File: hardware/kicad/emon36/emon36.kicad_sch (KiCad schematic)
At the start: 39 parts, among them J1 Barrel_Jack, J37 USB_B_Micro, SW1 SW_MEC_5E, SW2 SW_MEC_5E, SW3 SW_MEC_5E, SW4 SW_MEC_5E, SW5 SW_MEC_5E, SW6 SW_MEC_5E, U1 ESP32-C3-WROOM-02-N4, U8 TPS54233

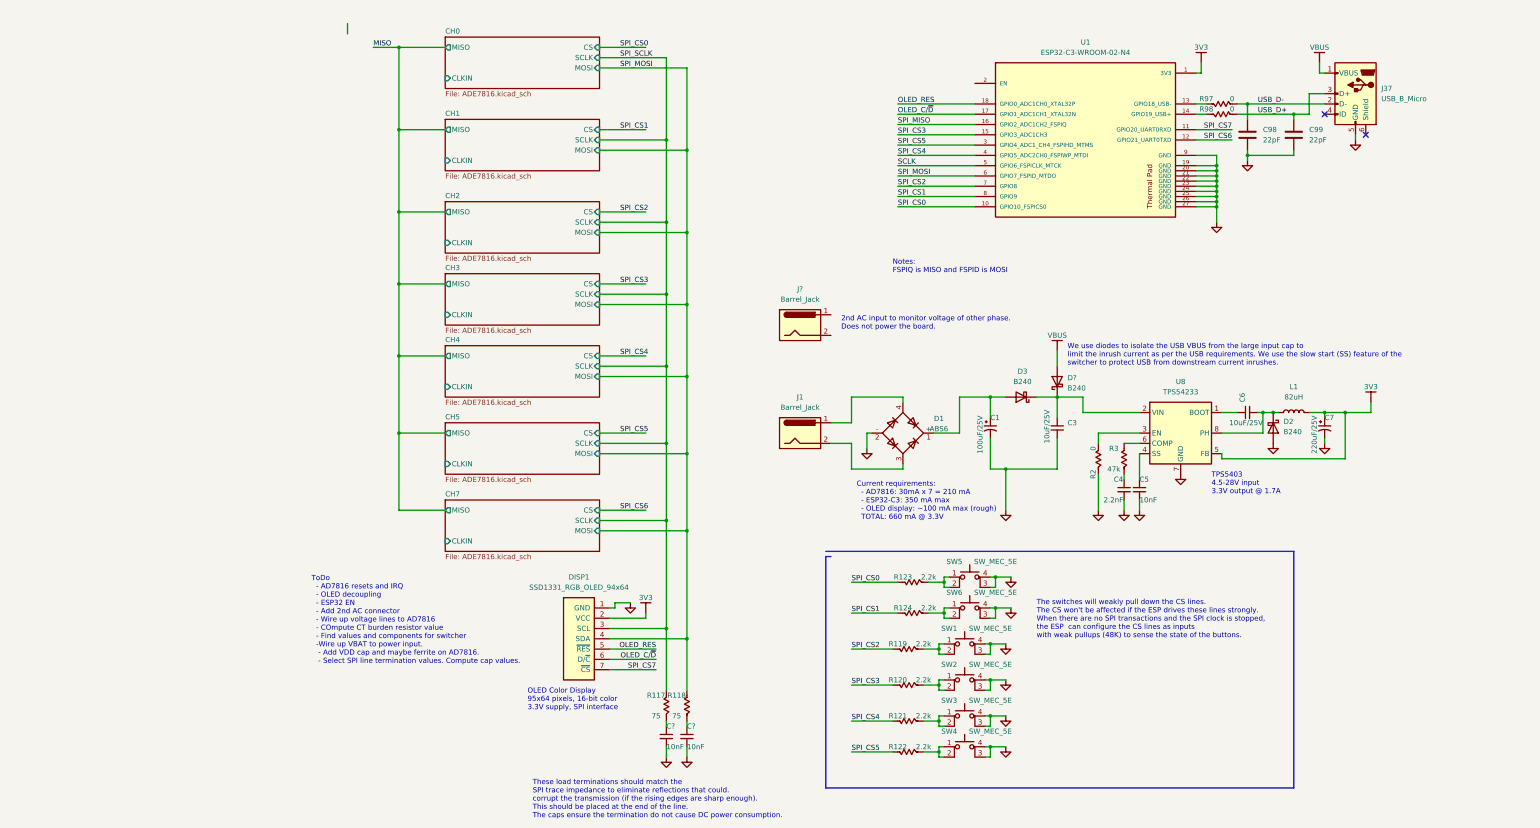
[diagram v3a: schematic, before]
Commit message: Another major schematics/PCB iteration. Added decoupling caps, interrupts, etc. Improved power system. Added clock.
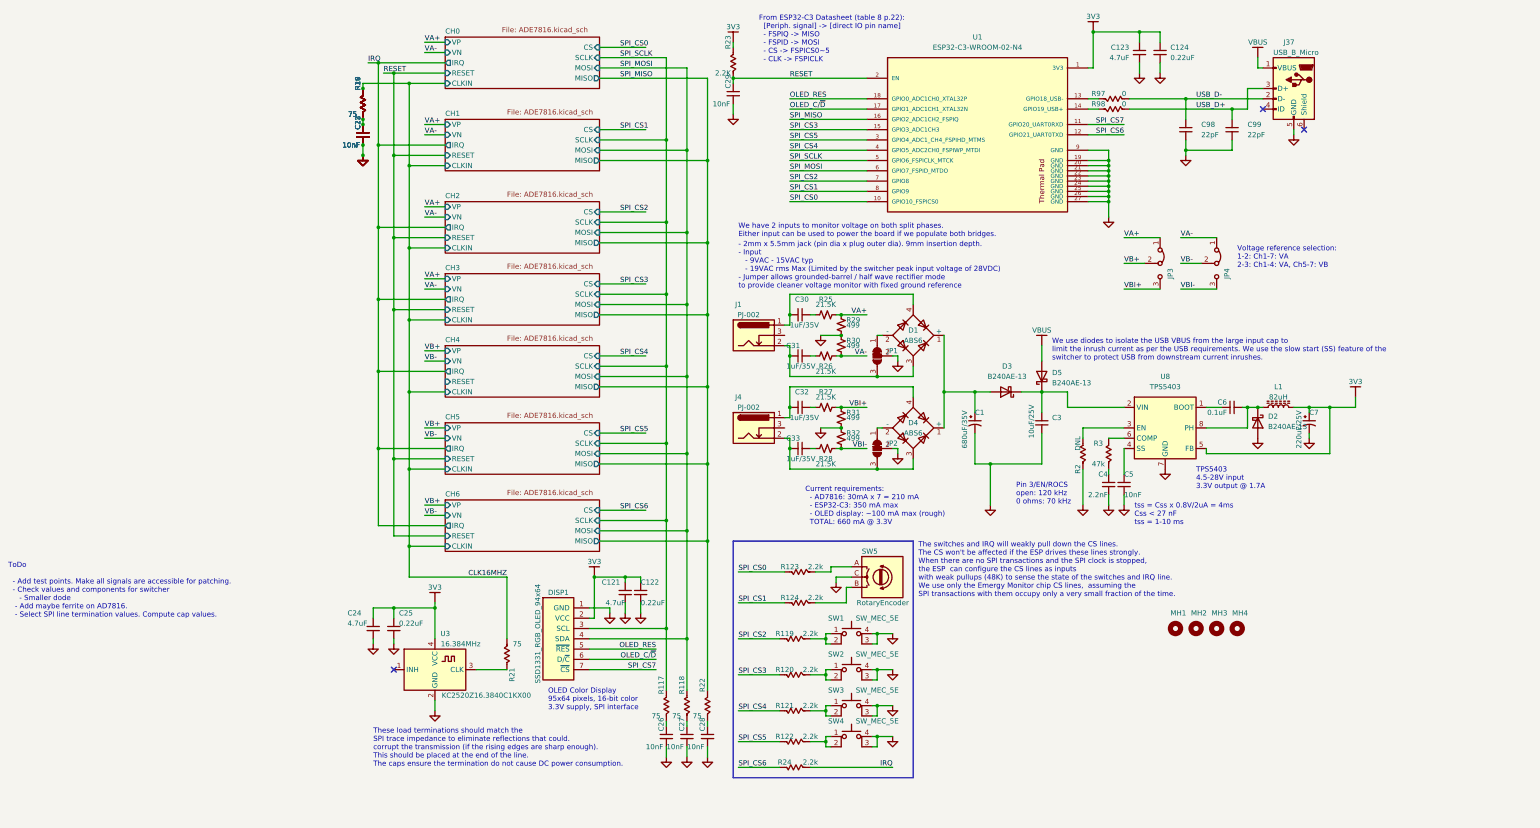
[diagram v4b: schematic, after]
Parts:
- removed J1, J?: Barrel_Jack, Connector_BarrelJack:BarrelJack_SwitchcraftConxall_RAPC10U_Horizontal, symbol Connector:Barrel_Jack
- removed SW5, SW6: SW_MEC_5E, Button_Switch_SMD:SW_Push_1P1T_NO_6x6mm_H13mm, symbol Switch:SW_MEC_5E
- added C121, C123, C24: 4.7uF, Capacitor_SMD:C_0603_1608Metric, symbol Device:C_Small
- added C122, C124, C25: 0.22uF, Capacitor_SMD:C_0603_1608Metric, symbol Device:C_Small
- added C18, C21, C22, C23, C28, C29: 10nF, Capacitor_SMD:C_0603_1608Metric, symbol Device:C_Small
- added C30, C31, C32, C33: 1uF/35V, Capacitor_SMD:C_0603_1608Metric, symbol Device:C_Small
- added D4: ABS6, Diode_SMD:Diode_Bridge_Diotec_ABS, symbol Diode_Bridge:ABS6
- added J1, J4: Barrel_Jack, Connector_BarrelJack:BarrelJack_Horizontal, symbol Connector:Barrel_Jack_Switch
- added JP1, JP2: SolderJumper_3_Bridged12, Jumper:SolderJumper-3_P1.3mm_Bridged12_RoundedPad1.0x1.5mm, symbol Jumper:SolderJumper_3_Bridged12
- added JP3, JP4: Jumper_3_Bridged12, Connector_PinHeader_2.54mm:PinHeader_1x03_P2.54mm_Vertical, symbol Jumper:Jumper_3_Bridged12
- added MH1, MH2, MH3, MH4: MountingHole, MountingHole:MountingHole_2.7mm_M2.5, symbol Mechanical:MountingHole
- added R17, R18, R19, R20, R21, R22: 75, Resistor_SMD:R_0603_1608Metric, symbol emon36:R_US
- added R23: 2.2K, Resistor_SMD:R_0603_1608Metric, symbol emon36:R_US
- added R24: 2.2k, Resistor_SMD:R_0603_1608Metric, symbol emon36:R_US
- added R25, R26, R27, R28: 21.5K, Resistor_SMD:R_0603_1608Metric, symbol Device:R_Small_US
- added R29, R30, R31, R32: 499, Resistor_SMD:R_0603_1608Metric, symbol Device:R_Small_US
- added SW5: RotaryEncoder, Rotary_Encoder:RotaryEncoder_Alps_EC12E_Vertical_H20mm, symbol Device:RotaryEncoder
- added U3: 16.384MHz, Oscillator:Oscillator_SMD_Kyocera_KC2520Z-4Pin_2.5x2.0mm, symbol Oscillator:KC2520Z
- C1: value 100uF/25V -> 680uF/35V
- C6: value 10uF/25V -> 0.1uF
- C98, C99: symbol Device:C -> Device:C_Small
- D1: MFR (none) -> Diotec; MPN (none) -> ABS6
- D2, D3: value B240 -> B240AE-13; footprint Diode_SMD:D_SMB -> Diode_SMD:D_SOD-123F; MFR (none) -> Diodes Inc; MPN (none) -> B240AE-13
- D5: renamed from D?; value B240 -> B240AE-13; footprint Diode_SMD:D_SMB -> Diode_SMD:D_SOD-123F; MFR (none) -> Diodes Inc; MPN (none) -> B240AE-13
- L1: footprint Inductor_THT:L_Radial_D7.5mm_P3.50mm_Fastron_07P -> Inductor_SMD:L_Bourns_SRN8040TA; symbol Device:L -> Device:L_Ferrite; MFR (none) -> Bourns; MPN (none) -> SRN8040TA-820M
- R2: value 0 -> DNL
- U1: MFR (none) -> Espressif Systems; MPN (none) -> ESP32-C3-WROOM-02-H4
- U8: value TPS54233 -> TPS5403
- gave numbers to parts that had none: 2
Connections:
- net SCLK is gone; now on net SPI_SCLK: U1.5 (GPIO6_FSPICLK_MTCK)
- net 3V3: now also C121.1, C122.1, C123.1, C124.1, C24.1, C25.1, R23.1, U3.4 (VCC)
- net GND: now also C121.2, C122.2, C123.2, C124.2, C18.2, C21.2, C22.2, C23.2, C24.2, C25.2, C28.2, C29.2, JP1.2 (C), JP2.2 (C), R29.2, R30.1, R31.2, R32.1, SW5.C, U3.2 (GND); no longer D1.2 (-)
- net SPI_CS6: now also R24.1
- net SPI_MISO: now also R22.1
- net at R124.2: now also SW5.B
- net at C1.1, D1.1 (+), D3.2 (A): now also D4.1 (+)
- net at D1.4: now also C30.2, J1.1
- net at D1.3: now also C31.1, J1.2, JP1.3 (B)
- net at R123.2: now also SW5.A
- net RESET: now reaches U1.2 (EN)
- net RESET: now also C29.1, R23.2
- new net: C30.1, R25.1
- new net: C18.1, C21.1, C22.1, C23.1, R17.2, R18.2, R19.2, R20.2
- new net: D1.2 (-), JP1.1 (A)
- new net: D4.2 (-), JP2.1 (A)
- new net: C33.1, D4.3, J4.2, JP2.3 (B)
- new net: C32.2, D4.4, J4.1
- new net: C32.1, R27.1
- new net: C31.2, R26.1
- new net: C28.1, R22.2
- new net: R21.1, U3.3 (CLK)
- new net: C33.2, R28.1
- new net CLK16MHZ: R17.1, R18.1, R19.1, R20.1, R21.2
- new net IRQ: R24.2
- new net VA+: JP3.1 (A), R25.2, R29.1
- new net VA-: JP4.1 (A), R26.2, R30.2
- new net VB+: JP3.2 (C)
- new net VB-: JP4.2 (C)
- new net VBI+: JP3.3 (B), R27.2, R31.1
- new net VBI-: JP4.3 (B), R28.2, R32.2
- no-connect marks 2 -> 3
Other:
- removed sheet CH7
- added sheet CH6 (ADE7816.kicad_sch)
- sheet CH0 ports: added IRQ, RESET, VN, VP; removed none
- sheet CH1 ports: added IRQ, RESET, VN, VP; removed none
- sheet CH2 ports: added IRQ, RESET, VN, VP; removed none
- sheet CH3 ports: added IRQ, RESET, VN, VP; removed none
- sheet CH4 ports: added IRQ, RESET, VN, VP; removed none
- sheet CH5 ports: added IRQ, RESET, VN, VP; removed none
- note added: "- 2mm x 5.5mm jack (pin dia x plug outer dia). 9mm insertion depth. - Input - 9VAC - 15VAC typ - 19VAC rms Max (Limited by the switcher peak input voltage of 28VDC) - Jumper allows grounded-barrel / half wave rectifier mode to provide cleaner voltage monitor with fixed ground reference"
- note added: "From ESP32-C3 Datasheet (table 8 p.22): [Periph. signal] -> [direct IO pin name] - FSPIQ -> MISO - FSPID -> MOSI - CS -> FSPICS0~5 - CLK -> FSPICLK"
- note added: "Pin 3/EN/ROCS open: 120 kHz 0 ohms: 70 kHz"
- note added: "The switches and IRQ will weakly pull down the CS lines. The CS won't be affected if the ESP drives these lines strongly. When there are no SPI transactions and the SPI clock is stopped, the ESP can configure the CS lines as inputs with weak pullups (48K) to sense the state of the switches and IRQ line. We use only the Emergy Monitor chip CS lines, assuming the SPI transactions with them occupy o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"
- note added: "ToDo - Add test points. Make all signals are accessible for patching. - Check values and components for switcher - Smaller dode - Add maybe ferrite on AD7816. - Select SPI line termination values. Compute cap values."
- note added: "Voltage reference selection: 1-2: Ch1-7: VA 2-3: Ch1-4: VA, Ch5-7: VB"
- note added: "We have 2 inputs to monitor voltage on both split phases. Either input can be used to power the board if we populate both bridges."
- note added: "tss = Css x 0.8V/2uA = 4ms Css < 27 nF tss = 1-10 ms"
- note removed: "2nd AC input to monitor voltage of other phase. Does not power the board."
- note removed: "Notes: FSPIQ is MISO and FSPID is MOSI"
- note removed: "The switches will weakly pull down the CS lines. The CS won't be affected if the ESP drives these lines strongly. When there are no SPI transactions and the SPI clock is stopped, the ESP can configure the CS lines as inputs with weak pullups (48K) to sense the state of the buttons."
- note removed: "ToDo - AD7816 resets and IRQ - OLED decoupling - ESP32 EN - Add 2nd AC connector - Wire up voltage lines to AD7816 - COmpute CT burden resistor value - Find values and components for switcher -Wire up VBAT to power input. - Add VDD cap and maybe ferrite on AD7816. - Select SPI line termination values. Compute cap values."
- company: (none) -> JFCInc
- title: (none) -> EMON36 - 36-channel single-board energy monitor
- moved on the sheet: C1, C3, C4, C5, C6, C7, C98, C99, D2, D3, D5, DISP1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

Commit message: Finished schematics, layout and routing. Ready for verification.
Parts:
- removed C121: 4.7uF, Capacitor_SMD:C_0603_1608Metric, symbol Device:C_Small
- removed C122: 0.22uF, Capacitor_SMD:C_0603_1608Metric, symbol Device:C_Small
- removed D1, D4: ABS6, Diode_SMD:Diode_Bridge_Diotec_ABS, symbol Diode_Bridge:ABS6
- removed JP1, JP2: SolderJumper_3_Bridged12, Jumper:SolderJumper-3_P1.3mm_Bridged12_RoundedPad1.0x1.5mm, symbol Jumper:SolderJumper_3_Bridged12
- removed JP3, JP4: Jumper_3_Bridged12, Connector_PinHeader_2.54mm:PinHeader_1x03_P2.54mm_Vertical, symbol Jumper:Jumper_3_Bridged12
- removed R118, R19, R20, R21, R22: 75, Resistor_SMD:R_0603_1608Metric, symbol emon36:R_US
- removed R26, R28: 21.5K, Resistor_SMD:R_0603_1608Metric, symbol Device:R_Small_US
- removed R30, R32: 499, Resistor_SMD:R_0603_1608Metric, symbol Device:R_Small_US
- removed SW1: SW_MEC_5E, Button_Switch_SMD:SW_Push_1P1T_NO_6x6mm_H13mm, symbol Switch:SW_MEC_5E
- removed SW5: RotaryEncoder, Rotary_Encoder:RotaryEncoder_Alps_EC12E_Vertical_H20mm, symbol Device:RotaryEncoder
- added D1, D4: B240AE-13, Diode_SMD:D_SOD-123F, symbol Diode:B240
- added H29, H30, H31, H32: MountingHole_Pad, _Connector_Audio_local:STX-4335_Combined_Mounting_Hole, symbol Mechanical:MountingHole_Pad
- added J17: Conn_02x03_Odd_Even, Connector_PinHeader_2.54mm:PinHeader_2x03_P2.54mm_Vertical, symbol Connector_Generic:Conn_02x03_Odd_Even
- added R19, R20: 21.5K, Resistor_SMD:R_0603_1608Metric, symbol Device:R_Small_US
- added R21, R22: 499, Resistor_SMD:R_0603_1608Metric, symbol Device:R_Small_US
- added RN1, RN2: 33, _SnapEDA Library:RESCAV50P200X100X55-8N, symbol Device:R_Network04_US
- added U11: PL133-97QC, emon36:PL133-97QC, symbol PL133-97QC:PL133-97QC
- added U12: PEC12R-4117F-S0012, _SnapEDA Library:ENC_PEC12R-4025F-S0024, symbol PEC12R-4025F-S0024:PEC12R-4025F-S0024
- C1: footprint Capacitor_Tantalum_SMD:CP_EIA-1608-08_AVX-J -> Capacitor_THT:CP_Radial_D10.0mm_P5.00mm; MFR (none) -> Panasonic; MPN (none) -> EEU-FR1V681LB
- C123, C24: value 4.7uF -> 4.7uF/10V; Desc (none) -> CAP CER 4.7UF 10V X7S 0603; MFR (none) -> TDK Corporation; MPN (none) -> C1608X7S1A475K080AC
- C18: value 10nF -> 0.1uF
- C21, C29: value 10nF -> 0.22uF
- C22: value 10nF -> 4.7uF/10V; Desc (none) -> CAP CER 4.7UF 10V X7S 0603; MFR (none) -> TDK Corporation; MPN (none) -> C1608X7S1A475K080AC
- C23, C26: value 10nF -> 100pF
- C27, C28: value 10nF -> 47nF
- C3: value 10uF/25V -> 10uF/50V; footprint Capacitor_SMD:C_0603_1608Metric -> Capacitor_SMD:C_1206_3216Metric; Desc (none) -> CAP CER 10UF 50V X7R 1206; MFR (none) -> Samsung; MPN (none) -> CL31B106KBHNNNE
- C30, C31: value 1uF/35V -> 47nF
- C32: value 1uF/35V -> 10uF/50V; footprint Capacitor_SMD:C_0603_1608Metric -> Capacitor_SMD:C_1206_3216Metric; Desc (none) -> CAP CER 10UF 50V X7R 1206; MFR (none) -> Samsung; MPN (none) -> CL31B106KBHNNNE
- C33: value 1uF/35V -> 0.1uF
- C7: value 220uF/25V -> 220uF/35V; footprint Capacitor_Tantalum_SMD:CP_EIA-1608-08_AVX-J -> Capacitor_THT:CP_Radial_D10.0mm_P5.00mm; MFR (none) -> Robycon; MPN (none) -> 35YXF220MEFC10X12.5
- J4: footprint Connector_BarrelJack:BarrelJack_Horizontal -> emon36:PJ-002A
- R117: value 75 -> 50
- R17, R18: value 75 -> 22
- SW2, SW3, SW4: footprint Button_Switch_SMD:SW_Push_1P1T_NO_6x6mm_H13mm -> _Button_Switch_SMD:SW_Push_1P1T_NO_6x6mm_H13mm; symbol Switch:SW_MEC_5E -> emon36:SW_MEC_5E; MFR (none) -> C&K; MPN (none) -> PTS645SK13SMTR92LFS
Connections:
- net 3V3: now also C18.1, C21.1, C22.1, C32.1, C33.2, U11.11 (VDD), U11.2 (VDD); no longer D5.2 (A), J37.1 (VBUS)
- net GND: now also C30.2, C31.2, C32.2, C33.1, J1.2, J4.2, U1.28 (GND), U1.29 (GND), U1.30 (GND), U1.31 (GND), U1.32 (GND), U1.33 (GND), U1.34 (GND), U1.35 (GND), U1.36 (GND), U1.37 (GND), H29.1, H30.1, H31.1, H32.1, R19.1, R20.1, R21.2, R22.2, U11.10 (GND), U11.17 (EPAD), U11.3 (GND), U11.7 (GND), U12.2 (S2), U12.C (COM)
- net SPI_MOSI: now also R18.2; no longer U1.6 (GPIO7_FSPID_MTDO)
- net SPI_SCLK: now also C23.1, R17.2; no longer U1.5 (GPIO6_FSPICLK_MTCK)
- net VA+: now also C27.1, J17.1 (Pin_1)
- net VA-: now also C28.1, J17.2 (Pin_2), R19.2, R21.1
- net VB+: now also J17.3 (Pin_3)
- net VB-: now also J17.4 (Pin_4)
- net VBI+: now also C30.1, J17.5 (Pin_5)
- net VBI-: now also C31.1, J17.6 (Pin_6), R20.2, R22.1
- net Vin: now reaches C3.1, D3.1 (K), D5.1 (K), U8.2 (VIN)
- net at R25.1: now also J1.1, D1.2 (A); no longer C30.1
- net at R123.2: now also U12.A (CHA)
- net at R124.2: now also U12.B (CHB)
- net Vrect: now reaches C1.1, D3.2 (A)
- net Vrect: now also D1.1 (K), D4.1 (K)
- net at J4.1: now also R27.1, D4.2 (A); no longer C32.2
- net SW_BOOT: now reaches C6.1, U8.1 (BOOT)
- net SW_EN: now reaches R2.1, U8.3 (EN)
- net SW_SS: now reaches C5.1, U8.4 (SS)
- net SW_COMP: now reaches R3.1, U8.6 (COMP)
- net SW_PH: now reaches C6.2, D2.1 (K), L1.1, U8.8 (PH)
- net at U3.3 (CLK): now also U11.15 (REF)
- net at R119.2: now also U12.1 (S1)
- net CLK16MHZ: no longer names the net of R18.1
- net CLK16MHZ: now also U1.6 (GPIO7_FSPID_MTDO); no longer R17.1
- new net: R17.1, U1.5 (GPIO6_FSPICLK_MTCK)
- new net CLK0: RN1.2 (R2)
- new net CLK0_R: RN1.7 (R7), U11.5 (CLK3)
- new net CLK1: RN1.3 (R3)
- new net CLK1_R: RN1.6 (R6), U11.8 (CLK4)
- new net CLK2: RN1.4 (R4)
- new net CLK2_R: RN1.5 (R5), U11.9 (CLK5)
- new net CLK3: RN2.4 (R4)
- new net CLK3_R: RN2.5 (R5), U11.1 (CLK1)
- new net CLK4: RN2.3 (R3)
- new net CLK4_R: RN2.6 (R6), U11.16 (CLK9)
- new net CLK5: RN2.2 (R2)
- new net CLK5_R: RN2.7 (R7), U11.13 (CLK7)
- new net CLK6: RN2.1 (R1)
- new net CLK6_R: RN2.8 (R8), U11.12 (CLK6)
- new net VBUS: D5.2 (A), J37.1 (VBUS)
- no-connect marks 3 -> 8
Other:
- note added: "16.384 MHz Clock"
- note added: "The AC termination shall be placed at the end of the multidrop clock line."
- note added: "ToDo - Add test points. Make all signals are accessible for patching. - Add maybe ferrite on AD7816. - Audio jack positioning"
- note added: "USB shields should be connected at the host only"
- note added: "User buttons"
- note added: "Voltage reference selection: 1-3 & 2-4: Ch1-7: VA 3-5 & 4-6: Ch1-4: VA, Ch5-7: VB"
- note added: "We use diodes to isolate the USB VBUS from the large input cap to limit the inrush current as per the USB requirements. We rely on the slow start (SS) feature of the switcher to protect USB from downstream current inrushes."
- note added: "or AI Thinker ESP-C3-13 (4M)"
- note removed: "These load terminations should match the SPI trace impedance to eliminate reflections that could. corrupt the transmission (if the rising edges are sharp enough). This should be placed at the end of the line. The caps ensure the termination do not cause DC power consumption."
- note removed: "ToDo - Add test points. Make all signals are accessible for patching. - Check values and components for switcher - Smaller dode - Add maybe ferrite on AD7816. - Select SPI line termination values. Compute cap values."
- note removed: "Voltage reference selection: 1-2: Ch1-7: VA 2-3: Ch1-4: VA, Ch5-7: VB"
- note removed: "We use diodes to isolate the USB VBUS from the large input cap to limit the inrush current as per the USB requirements. We use the slow start (SS) feature of the switcher to protect USB from downstream current inrushes."
- moved on the sheet: C1, C123, C124, C24, C25, C26, C29, C3, C98, C99, D3, D5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
